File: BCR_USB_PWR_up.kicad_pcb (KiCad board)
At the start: 2 copper layers, 13.3 x 14.1 mm, 2 parts, among them CN1 DB9_Female, CN2 UE27AC54100

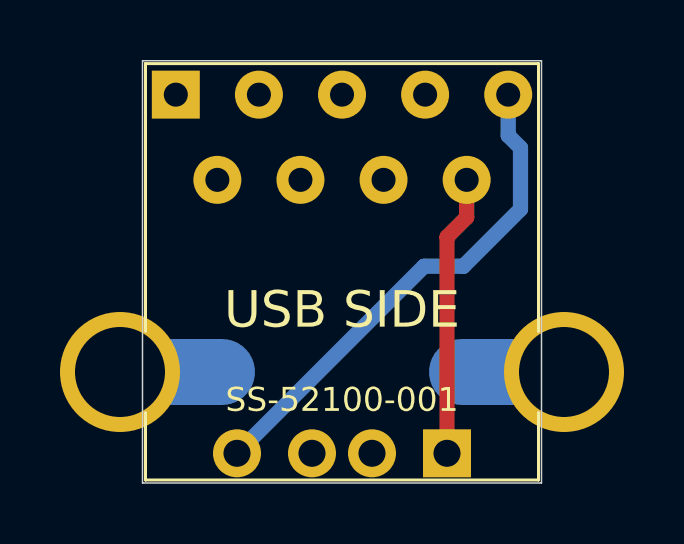
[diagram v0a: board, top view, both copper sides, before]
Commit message: db9 pin 7 is the real GND, not pin 5
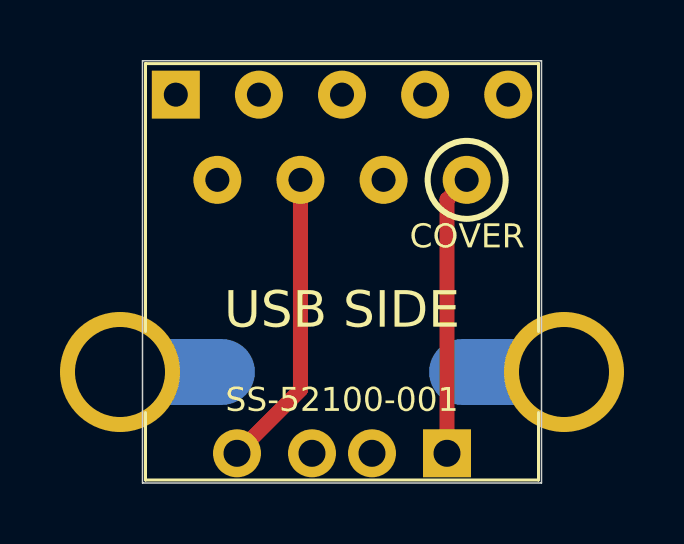
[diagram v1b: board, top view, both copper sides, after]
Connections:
- CN1 pad 5: /GND -> (no net)
- CN1 pad 7: (no net) -> /GND
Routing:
- net /GND: track 16.8 -> 9.99 mm
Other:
- net class Default: clearance 0.2 -> 0.16; trace_width 0.25 -> 0.16; via_dia 0.8 -> 0.42; via_drill 0.4 -> 0.26
- rule trace_clearance: 0.2 -> 0.16
- rule trace_min: 0.2 -> 0.16
- rule via_min_drill: 0.3 -> 0.26
- rule via_min_size: 0.4 -> 0.42
- board text added: "COVER"
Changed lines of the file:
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@@
   (general
     (thickness 1.6)
-    (drawings 14)
-    (tracks 9)
+    (drawings 16)
+    (tracks 4)
     (zones 0)
     (modules 2)
@@
   )
   (setup
-    (last_trace_width 0.25)
-    (user_trace_width 0.508)
-    (trace_clearance 0.2)
+    (last_trace_width 0.5)
+    (user_trace_width 0.5)
+    (trace_clearance 0.16)
     (zone_clearance 0.508)
     (zone_45_only no)
-    (trace_min 0.2)
-    (via_size 0.8)
-    (via_drill 0.4)
-    (via_min_size 0.4)
-    (via_min_drill 0.3)
-    (user_via 0.508 0.3048)
+    (trace_min 0.16)
+    (via_size 0.42)
+    (via_drill 0.26)
+    (via_min_size 0.42)
+    (via_min_drill 0.26)
     (uvia_size 0.3)
     (uvia_drill 0.1)
@@
     (mod_text_width 0.15)
     (pad_size 1.6 1.6)
-    (pad_drill 0.9)
+    (pad_drill 0.8)
     (pad_to_mask_clearance 0)
     (aux_axis_origin 0 0)
@@
   (net 3 "Net-(CN2-PadSH)")
   (net_class Default "This is the default net class."
-    (clearance 0.2)
-    (trace_width 0.25)
-    (via_dia 0.8)
-    (via_drill 0.4)
+    (clearance 0.16)
+    (trace_width 0.16)
+    (via_dia 0.42)
+    (via_drill 0.26)
     (uvia_dia 0.3)
     (uvia_drill 0.1)
@@
       (effects (font (size 1 1) (thickness 0.15)))
     )
+    (fp_line (start -6.55 -3.6) (end 6.55 -3.6) (layer F.SilkS) (width 0.1))
+    (fp_line (start 6.55 1.35) (end 6.55 10.28) (layer F.SilkS) (width 0.1))
+    (fp_line (start -6.55 1.35) (end -6.55 10.28) (layer F.SilkS) (width 0.1))
+    (fp_line (start -6.55 -3.6) (end -6.55 -1.35) (layer F.SilkS) (width 0.1))
+    (fp_line (start -6.55 -3.6) (end 6.55 -3.6) (layer F.Fab) (width 0.1))
+    (fp_line (start 6.55 -3.6) (end 6.55 10.28) (layer F.Fab) (width 0.1))
+    (fp_line (start -6.55 -3.6) (end -6.55 10.28) (layer F.Fab) (width 0.1))
+    (fp_line (start -6.55 10.28) (end 6.55 10.28) (layer F.Fab) (width 0.1))
+    (fp_line (start 6.55 -3.6) (end 6.55 -1.35) (layer F.SilkS) (width 0.1))
+    (fp_line (start 6.55 10.28) (end -6.55 10.28) (layer F.SilkS) (width 0.1))
+    (fp_line (start -6.75 -3.94) (end 6.75 -3.94) (layer F.CrtYd) (width 0.05))
+    (fp_line (start 6.75 -3.94) (end 6.75 10.375) (layer F.CrtYd) (width 0.05))
+    (fp_line (start -6.75 -3.94) (end -6.75 10.375) (layer F.CrtYd) (width 0.05))
     (fp_line (start -6.75 10.375) (end 6.75 10.375) (layer F.CrtYd) (width 0.05))
-    (fp_line (start -6.75 -3.94) (end -6.75 10.375) (layer F.CrtYd) (width 0.05))
-    (fp_line (start 6.75 -3.94) (end 6.75 10.375) (layer F.CrtYd) (width 0.05))
-    (fp_line (start -6.75 -3.94) (end 6.75 -3.94) (layer F.CrtYd) (width 0.05))
-    (fp_line (start 6.55 10.28) (end -6.55 10.28) (layer F.SilkS) (width 0.1))
-    (fp_line (start 6.55 -3.6) (end 6.55 -1.35) (layer F.SilkS) (width 0.1))
-    (fp_line (start -6.55 10.28) (end 6.55 10.28) (layer F.Fab) (width 0.1))
-    (fp_line (start -6.55 -3.6) (end -6.55 10.28) (layer F.Fab) (width 0.1))
-    (fp_line (start 6.55 -3.6) (end 6.55 10.28) (layer F.Fab) (width 0.1))
-    (fp_line (start -6.55 -3.6) (end 6.55 -3.6) (layer F.Fab) (width 0.1))
-    (fp_line (start -6.55 -3.6) (end -6.55 -1.35) (layer F.SilkS) (width 0.1))
-    (fp_line (start -6.55 1.35) (end -6.55 10.28) (layer F.SilkS) (width 0.1))
-    (fp_line (start 6.55 1.35) (end 6.55 10.28) (layer F.SilkS) (width 0.1))
-    (fp_line (start -6.55 -3.6) (end 6.55 -3.6) (layer F.SilkS) (width 0.1))
     (fp_text user %R (at -0.025 0.975 180) (layer F.Fab)
       (effects (font (size 1 1) (thickness 0.15)))
@@
       (effects (font (size 1 1) (thickness 0.15)) (justify mirror))
     )
+    (fp_line (start -6.54 -1.42) (end -4.54 -1.42) (layer Dwgs.User) (width 0.01))
+    (fp_line (start -5.54 -0.82) (end -5.54 -2.02) (layer Dwgs.User) (width 0.01))
+    (fp_line (start -11.783194 2.53) (end 0.703194 2.53) (layer B.Fab) (width 0.1))
+    (fp_line (start -10.954457 -5.37) (end -0.125543 -5.37) (layer B.Fab) (width 0.1))
+    (fp_line (start 2.278887 0.652163) (end 1.45015 -4.047837) (layer B.Fab) (width 0.1))
+    (fp_line (start -13.358887 0.652163) (end -12.53015 -4.047837) (layer B.Fab) (width 0.1))
+    (fp_line (start -11.771689 2.59) (end 0.691689 2.59) (layer B.SilkS) (width 0.12))
+    (fp_line (start -10.942952 -5.43) (end -0.137048 -5.43) (layer B.SilkS) (width 0.12))
+    (fp_line (start 2.32647 0.641744) (end 1.497733 -4.058256) (layer B.SilkS) (width 0.12))
+    (fp_line (start -13.40647 0.641744) (end -12.577733 -4.058256) (layer B.SilkS) (width 0.12))
+    (fp_line (start -13.95 3.91) (end -13.95 -6.74) (layer B.CrtYd) (width 0.05))
+    (fp_line (start -13.95 -6.74) (end 2.9 -6.74) (layer B.CrtYd) (width 0.05))
+    (fp_line (start 2.9 -6.74) (end 2.9 3.91) (layer B.CrtYd) (width 0.05))
     (fp_line (start 2.9 3.91) (end -13.95 3.91) (layer B.CrtYd) (width 0.05))
-    (fp_line (start 2.9 -6.74) (end 2.9 3.91) (layer B.CrtYd) (width 0.05))
-    (fp_line (start -13.95 -6.74) (end 2.9 -6.74) (layer B.CrtYd) (width 0.05))
-    (fp_line (start -13.95 3.91) (end -13.95 -6.74) (layer B.CrtYd) (width 0.05))
-    (fp_line (start -13.40647 0.641744) (end -12.577733 -4.058256) (layer B.SilkS) (width 0.12))
-    (fp_line (start 2.32647 0.641744) (end 1.497733 -4.058256) (layer B.SilkS) (width 0.12))
-    (fp_line (start -10.942952 -5.43) (end -0.137048 -5.43) (layer B.SilkS) (width 0.12))
-    (fp_line (start -11.771689 2.59) (end 0.691689 2.59) (layer B.SilkS) (width 0.12))
-    (fp_line (start -13.358887 0.652163) (end -12.53015 -4.047837) (layer B.Fab) (width 0.1))
-    (fp_line (start 2.278887 0.652163) (end 1.45015 -4.047837) (layer B.Fab) (width 0.1))
-    (fp_line (start -10.954457 -5.37) (end -0.125543 -5.37) (layer B.Fab) (width 0.1))
-    (fp_line (start -11.783194 2.53) (end 0.703194 2.53) (layer B.Fab) (width 0.1))
-    (fp_line (start -5.54 -0.82) (end -5.54 -2.02) (layer Dwgs.User) (width 0.01))
-    (fp_line (start -6.54 -1.42) (end -4.54 -1.42) (layer Dwgs.User) (width 0.01))
     (fp_text user %R (at -5.54 -1.42 180) (layer B.Fab)
       (effects (font (size 1 1) (thickness 0.15)) (justify mirror))
@@
       (net 1 /+5V))
     (pad 8 thru_hole circle (at -6.925 -2.84 180) (size 1.6 1.6) (drill 0.8) (layers *.Cu *.Mask))
-    (pad 7 thru_hole circle (at -4.155 -2.84 180) (size 1.6 1.6) (drill 0.8) (layers *.Cu *.Mask))
+    (pad 7 thru_hole circle (at -4.155 -2.84 180) (size 1.6 1.6) (drill 0.8) (layers *.Cu *.Mask)
+      (net 2 /GND))
     (pad 6 thru_hole circle (at -1.385 -2.84 180) (size 1.6 1.6) (drill 0.8) (layers *.Cu *.Mask))
-    (pad 5 thru_hole circle (at -11.08 0 180) (size 1.6 1.6) (drill 0.8) (layers *.Cu *.Mask)
-      (net 2 /GND))
+    (pad 5 thru_hole circle (at -11.08 0 180) (size 1.6 1.6) (drill 0.8) (layers *.Cu *.Mask))
     (pad 4 thru_hole circle (at -8.31 0 180) (size 1.6 1.6) (drill 0.8) (layers *.Cu *.Mask))
     (pad 3 thru_hole circle (at -5.54 0 180) (size 1.6 1.6) (drill 0.8) (layers *.Cu *.Mask))
@@
     )
   )
+  (gr_text COVER (at 131.17 99.058) (layer F.SilkS)
+    (effects (font (size 0.8 0.8) (thickness 0.1)))
+  )
+  (gr_circle (center 131.15526 97.17814) (end 132.45526 97.17814) (layer F.SilkS) (width 0.2))
   (gr_text "TE 5207826" (at 127 95.783) (layer B.SilkS)
     (effects (font (size 0.8 0.8) (thickness 0.1)) (justify mirror))
@@
     (effects (font (size 1.2192 1.2192) (thickness 0.2032)))
   )
-  (segment (start 130.5 99.083) (end 130.5 106.293) (width 0.508) (layer F.Cu) (net 1))
-  (segment (start 131.15526 97.17814) (end 131.15526 98.42774) (width 0.508) (layer F.Cu) (net 1))
-  (segment (start 131.15526 98.42774) (end 130.5 99.083) (width 0.508) (layer F.Cu) (net 1))
-  (segment (start 132.54026 95.69826) (end 132.54026 94.33814) (width 0.508) (layer B.Cu) (net 2))
-  (segment (start 129.735 100.058) (end 131.05 100.058) (width 0.508) (layer B.Cu) (net 2))
-  (segment (start 132.95 98.158) (end 132.95 96.108) (width 0.508) (layer B.Cu) (net 2))
-  (segment (start 123.5 106.293) (end 129.735 100.058) (width 0.508) (layer B.Cu) (net 2))
-  (segment (start 131.05 100.058) (end 132.95 98.158) (width 0.508) (layer B.Cu) (net 2))
-  (segment (start 132.95 96.108) (end 132.54026 95.69826) (width 0.508) (layer B.Cu) (net 2))
+  (segment (start 130.5 97.8334) (end 130.5 106.293) (width 0.5) (layer F.Cu) (net 1))
+  (segment (start 131.15526 97.17814) (end 130.5 97.8334) (width 0.5) (layer F.Cu) (net 1))
+  (segment (start 125.61526 104.17774) (end 125.61526 97.17814) (width 0.5) (layer F.Cu) (net 2))
+  (segment (start 123.5 106.293) (end 125.61526 104.17774) (width 0.5) (layer F.Cu) (net 2))
 )
